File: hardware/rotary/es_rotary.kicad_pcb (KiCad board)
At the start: 2 copper layers, 38.1 x 38.1 mm, 6 parts, among them J1 T3_Left, J2 T3_Right

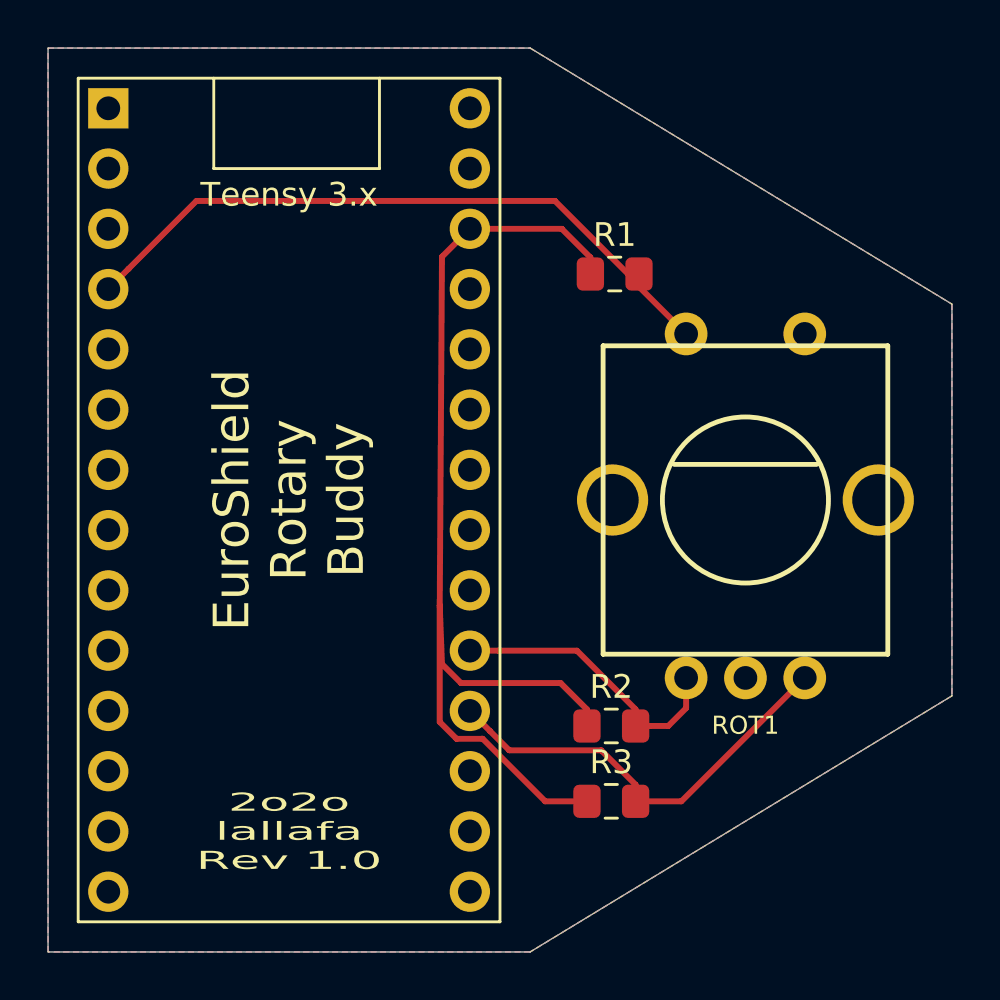
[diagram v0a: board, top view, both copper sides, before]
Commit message: updated rot and display to v1.1
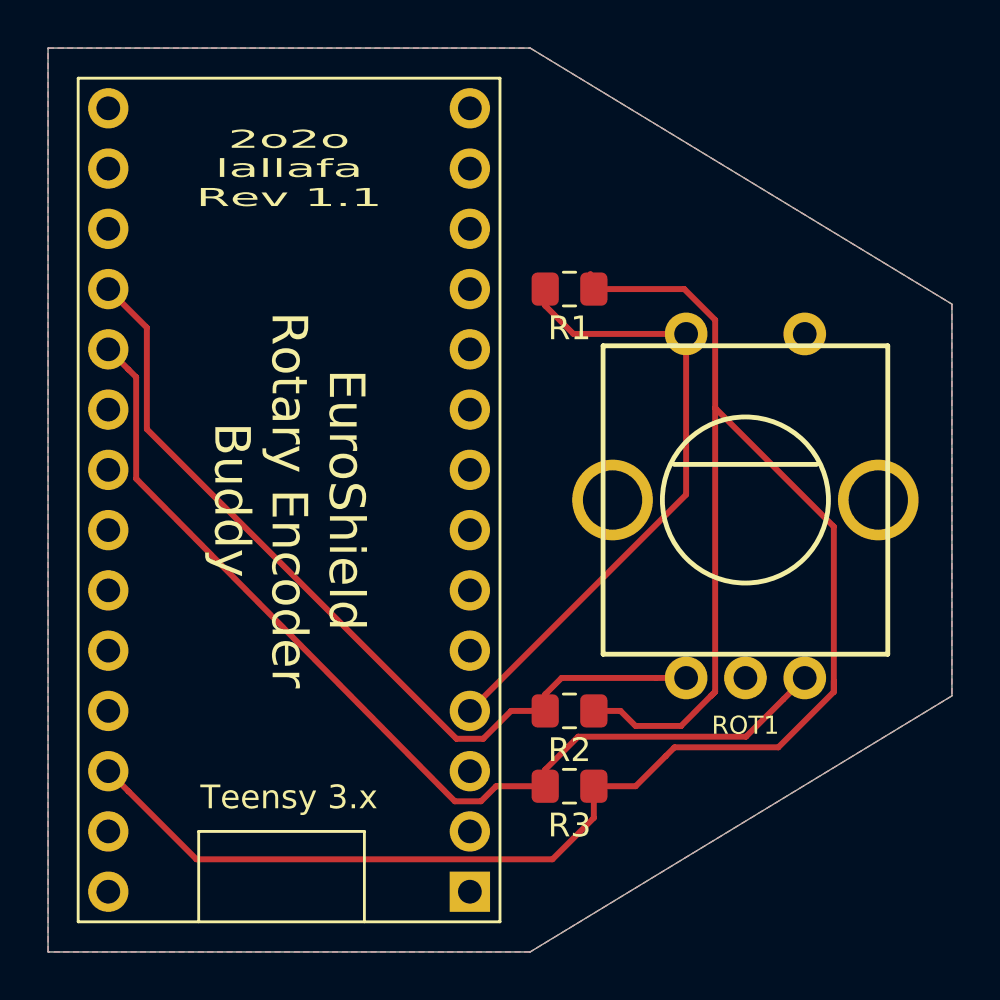
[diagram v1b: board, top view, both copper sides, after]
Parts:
- ROT1: footprint sparkfun:SF-ROTARY-ENCODER -> cvparts:Rotary_Encoder_PEC12R-3220F-S0024
- moved J1 36.4 mm to (149.9, 104.1), turned to 180 degrees
- moved J2 36.4 mm to (134.6, 104.1), turned to 180 degrees
- moved R1 2.01 mm to (154.1, 78.7), turned to 180 degrees
- moved R2 1.87 mm to (154.1, 96.5), turned to 180 degrees
- moved R3 1.87 mm to (154.1, 99.7), turned to 180 degrees
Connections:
- R2 pad 2: /ENC_A -> /ENC_B
- R3 pad 2: /ENC_B -> /ENC_A
- ROT1 pad 2: /ENC_A -> /ENC_B
- ROT1 pad 4: /ENC_B -> /ENC_A
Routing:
- net +3V3: track 45.2 -> 78.6 mm
- net /ENC_A: track 12.4 -> 42.4 mm
- net /ENC_B: track 18.3 -> 36.2 mm
- net /BUTTON: track 28.5 -> 26.8 mm
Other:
- board text added: "2o2o lallafa Rev 1.1"
- board text added: "EuroShield Rotary Encoder Buddy"
- board text removed: "2o2o lallafa Rev 1.0"
- board text removed: "EuroShield Rotary Buddy"

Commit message: set license: CC-BY-SA-4.0
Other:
- board text added: "CC-BY-SA 4.0"
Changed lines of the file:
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@@
   (general
     (thickness 1.6)
-    (drawings 16)
+    (drawings 17)
     (tracks 51)
     (zones 0)
@@
   (page A4)
   (layers
-    (0 F.Cu signal hide)
-    (31 B.Cu signal hide)
+    (0 F.Cu signal)
+    (31 B.Cu signal)
     (32 B.Adhes user hide)
     (33 F.Adhes user hide)
@@
     )
   )
+  (gr_text "CC-BY-SA\n4.0\n" (at 142.24 96.52) (layer F.SilkS)
+    (effects (font (size 1 1) (thickness 0.2)))
+  )
   (gr_line (start 170.18 95.885) (end 152.4 106.68) (layer Edge.Cuts) (width 0.05))
   (gr_line (start 170.18 79.375) (end 170.18 95.885) (layer Edge.Cuts) (width 0.05))
@@
     (effects (font (size 0.762 1.5) (thickness 0.1905)))
   )
-  (gr_text "EuroShield\nRotary Encoder\nBuddy" (at 142.24 87.63 270) (layer F.SilkS)
+  (gr_text "EuroShield\nRotary Encoder\nBuddy" (at 142.24 85.09 270) (layer F.SilkS)
     (effects (font (size 1.5 1.5) (thickness 0.3)))
   )
